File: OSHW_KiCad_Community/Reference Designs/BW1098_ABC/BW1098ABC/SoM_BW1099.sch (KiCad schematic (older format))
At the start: 29 parts

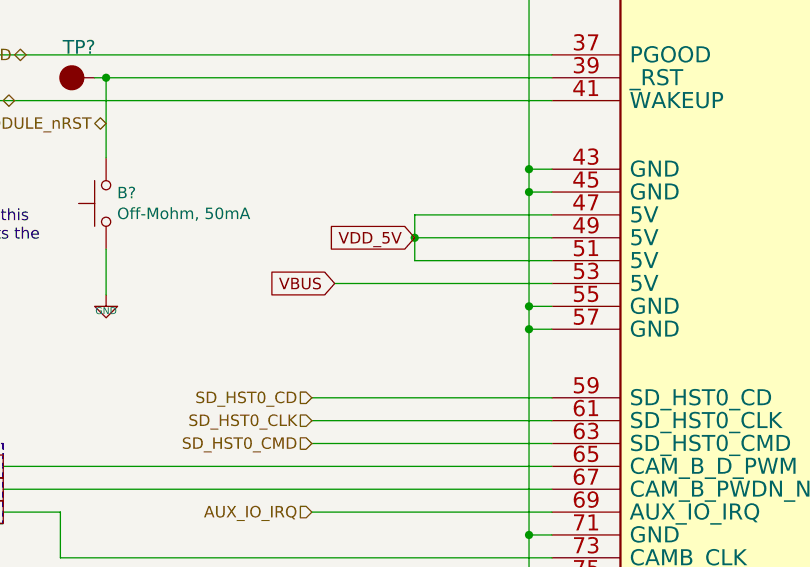
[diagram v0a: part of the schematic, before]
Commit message: skeleton complete, most footprints assigned, still need to check the transferred ones for dims
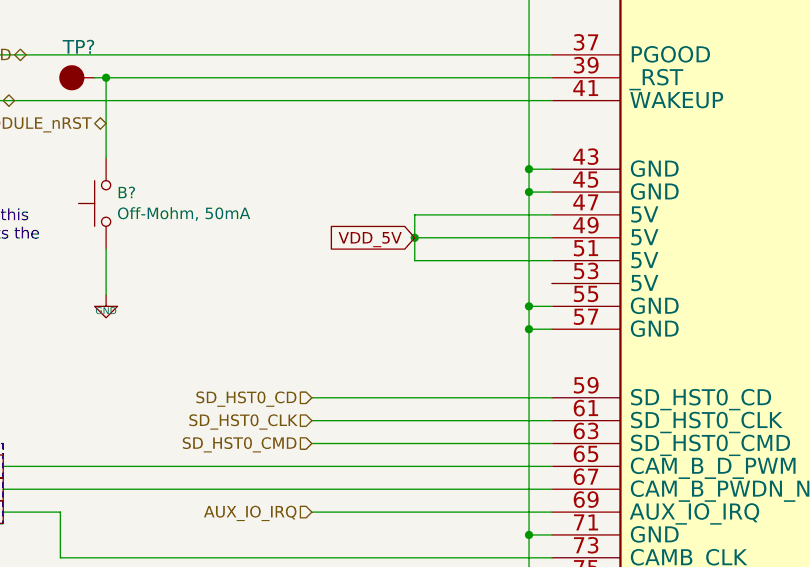
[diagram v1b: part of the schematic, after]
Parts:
- C?: footprint 0603 -> Capacitor_SMD:C_0201_0603Metric
- D? (x3): footprint (none) -> Diode_SMD:D_0201_0603Metric
- D?: footprint (none) -> Diode_SMD:D_SOD-523
- R? (x4): footprint (none) -> Resistor_SMD:R_0402_1005Metric
- R? (x2): footprint 0603 -> Resistor_SMD:R_0603_1608Metric
- TP? (x5): value BW1098OBC_Power_Supply-SchDoc-rescue_TEST_POINT- -> TEST_POINT; footprint (none) -> TestPoint:TestPoint_Loop_D1.80mm_Drill1.0mm_Beaded
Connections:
- net VBUS: no longer names the net of J?.53 (5V)
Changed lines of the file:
@@
 $Descr A3 16535 11693
 encoding utf-8
-Sheet 2 5
+Sheet 2 6
 Title ""
 Date ""
@@
 Wire Wire Line
 	7250 7600 4850 7600
-Wire Wire Line
-	6300 6000 7250 6000
 Wire Wire Line
 	10750 2900 9650 2900
@@
 AR Path="/5FF8D9B2/6009EFCC" Ref="TP?"  Part="1"
 F 0 "TP?" V 4283 5068 60  0000 C CNN
-F 1 "BW1098OBC_Power_Supply-SchDoc-rescue_TEST_POINT-" H 4230 5015 60  0001 L CNN
-F 2 "" H 4150 5000 60  0001 C CNN
+F 1 "TEST_POINT" H 4230 5015 60  0001 L CNN
+F 2 "TestPoint:TestPoint_Loop_D1.80mm_Drill1.0mm_Beaded" H 4150 5000 60  0001 C CNN
 F 3 "" H 4150 5000 60  0000 C CNN
 	1    4150 5000
@@
 AR Path="/5FF8D9B2/6009EFD2" Ref="TP?"  Part="1"
 F 0 "TP?" V 4283 5268 60  0000 C CNN
-F 1 "BW1098OBC_Power_Supply-SchDoc-rescue_TEST_POINT-" H 4230 5215 60  0001 L CNN
-F 2 "" H 4150 5200 60  0001 C CNN
+F 1 "TEST_POINT" H 4230 5215 60  0001 L CNN
+F 2 "TestPoint:TestPoint_Loop_D1.80mm_Drill1.0mm_Beaded" H 4150 5200 60  0001 C CNN
 F 3 "" H 4150 5200 60  0000 C CNN
 	1    4150 5200
@@
 AR Path="/5FF8D9B2/6009EFD8" Ref="TP?"  Part="1"
 F 0 "TP?" V 5383 5168 60  0000 C CNN
-F 1 "BW1098OBC_Power_Supply-SchDoc-rescue_TEST_POINT-" H 5330 5115 60  0001 L CNN
-F 2 "" H 5250 5100 60  0001 C CNN
+F 1 "TEST_POINT" H 5330 5115 60  0001 L CNN
+F 2 "TestPoint:TestPoint_Loop_D1.80mm_Drill1.0mm_Beaded" H 5250 5100 60  0001 C CNN
 F 3 "" H 5250 5100 60  0000 C CNN
 	1    5250 5100
@@
 AR Path="/5FF8D9B2/6009EFDE" Ref="TP?"  Part="1"
 F 0 "TP?" V 10250 6180 60  0000 L CNN
-F 1 "BW1098OBC_Power_Supply-SchDoc-rescue_TEST_POINT-" H 10330 6015 60  0001 L CNN
-F 2 "" H 10250 6000 60  0001 C CNN
+F 1 "TEST_POINT" H 10330 6015 60  0001 L CNN
+F 2 "TestPoint:TestPoint_Loop_D1.80mm_Drill1.0mm_Beaded" H 10250 6000 60  0001 C CNN
 F 3 "" H 10250 6000 60  0000 C CNN
 	1    10250 6000
@@
 F 0 "D?" V 1939 7632 50  0000 R CNN
 F 1 "ORANGE0603" V 1848 7632 50  0000 R CNN
-F 2 "" H 1900 7750 50  0001 C CNN
+F 2 "Diode_SMD:D_0201_0603Metric" H 1900 7750 50  0001 C CNN
 F 3 "~" H 1900 7750 50  0001 C CNN
 	1    1900 7750
@@
 F 0 "R?" H 1968 7396 50  0000 L CNN
 F 1 "1k 0402" H 1968 7305 50  0000 L CNN
-F 2 "" H 1900 7350 50  0001 C CNN
+F 2 "Resistor_SMD:R_0402_1005Metric" H 1900 7350 50  0001 C CNN
 F 3 "~" H 1900 7350 50  0001 C CNN
 	1    1900 7350
@@
 F 0 "D?" V 1889 5782 50  0000 R CNN
 F 1 "ORANGE0603" V 1798 5782 50  0000 R CNN
-F 2 "" H 1850 5900 50  0001 C CNN
+F 2 "Diode_SMD:D_0201_0603Metric" H 1850 5900 50  0001 C CNN
 F 3 "~" H 1850 5900 50  0001 C CNN
 	1    1850 5900
@@
 F 0 "R?" H 1918 5546 50  0000 L CNN
 F 1 "1k 0402" H 1918 5455 50  0000 L CNN
-F 2 "" H 1850 5500 50  0001 C CNN
+F 2 "Resistor_SMD:R_0402_1005Metric" H 1850 5500 50  0001 C CNN
 F 3 "~" H 1850 5500 50  0001 C CNN
 	1    1850 5500
@@
 F 0 "D?" V 1889 3482 50  0000 R CNN
 F 1 "RED0603" V 1798 3482 50  0000 R CNN
-F 2 "" H 1850 3600 50  0001 C CNN
+F 2 "Diode_SMD:D_0201_0603Metric" H 1850 3600 50  0001 C CNN
 F 3 "~" H 1850 3600 50  0001 C CNN
 	1    1850 3600
@@
 F 0 "R?" H 1918 3246 50  0000 L CNN
 F 1 "1k 0402" H 1918 3155 50  0000 L CNN
-F 2 "" H 1850 3200 50  0001 C CNN
+F 2 "Resistor_SMD:R_0402_1005Metric" H 1850 3200 50  0001 C CNN
 F 3 "~" H 1850 3200 50  0001 C CNN
 	1    1850 3200
@@
 F 0 "R?" H 1418 3146 50  0000 L CNN
 F 1 "1k 0402" H 1418 3055 50  0000 L CNN
-F 2 "" H 1350 3100 50  0001 C CNN
+F 2 "Resistor_SMD:R_0402_1005Metric" H 1350 3100 50  0001 C CNN
 F 3 "~" H 1350 3100 50  0001 C CNN
 	1    1350 3100
@@
 AR Path="/5FF8D9B2/6009F090" Ref="TP?"  Part="1"
 F 0 "TP?" H 10850 5350 60  0000 R CNN
-F 1 "BW1098OBC_Power_Supply-SchDoc-rescue_TEST_POINT-" H 11030 5215 60  0001 L CNN
-F 2 "" H 10950 5200 60  0001 C CNN
+F 1 "TEST_POINT" H 11030 5215 60  0001 L CNN
+F 2 "TestPoint:TestPoint_Loop_D1.80mm_Drill1.0mm_Beaded" H 10950 5200 60  0001 C CNN
 F 3 "" H 10950 5200 60  0000 C CNN
 	1    10950 5200
@@
 Text GLabel 4850 7000 0    50   UnSpc ~ 0
 CAM_B_CLK_OUT
-Text GLabel 6300 6000 0    50   Input ~ 0
-VBUS
 Text GLabel 6650 5800 0    50   Input ~ 0
 VDD_5V
@@
 F 0 "D?" H 13250 1143 50  0000 C CNN
 F 1 "BAS16XV2T1G" H 13250 1234 50  0000 C CNN
-F 2 "" H 13250 1275 50  0001 C CNN
-F 3 "" H 13250 1450 50  0001 C CNN
+F 2 "Diode_SMD:D_SOD-523" H 13250 1275 50  0001 C CNN
+F 3 "https://www.onsemi.com/pub/Collateral/BAS16XV2T1-D.PDF" H 13250 1450 50  0001 C CNN
 F 4 "DNP" H 13250 1325 50  0000 C CNN "Population"
 	1    13250 1450
@@
 F 0 "R?" V 13363 1718 45  0000 L CNN
 F 1 "10KOHM-0603" V 13550 1100 45  0000 L CNN
-F 2 "0603" H 13450 1800 20  0001 C CNN
+F 2 "Resistor_SMD:R_0603_1608Metric" H 13450 1800 20  0001 C CNN
 F 3 "" H 13450 1650 60  0001 C CNN
 F 4 "RES-00824" V 13534 1718 60  0001 L CNN "Field4"
@@
 F 0 "C?" H 14758 1995 45  0000 L CNN
 F 1 "4.7UF0603" H 14758 1911 45  0000 L CNN
-F 2 "0603" H 14650 2100 20  0001 C CNN
+F 2 "Capacitor_SMD:C_0201_0603Metric" H 14650 2100 20  0001 C CNN
 F 3 "" H 14650 1850 50  0001 C CNN
 F 4 "CAP-08280" H 14758 1816 60  0000 L CNN "Field4"
@@
 F 0 "R?" V 14650 1300 45  0000 L CNN
 F 1 "10KOHM-0603" V 14750 900 45  0000 L CNN
-F 2 "0603" H 14650 1600 20  0001 C CNN
+F 2 "Resistor_SMD:R_0603_1608Metric" H 14650 1600 20  0001 C CNN
 F 3 "" H 14650 1450 60  0001 C CNN
 F 4 "RES-00824" V 14734 1518 60  0001 L CNN "Field4"

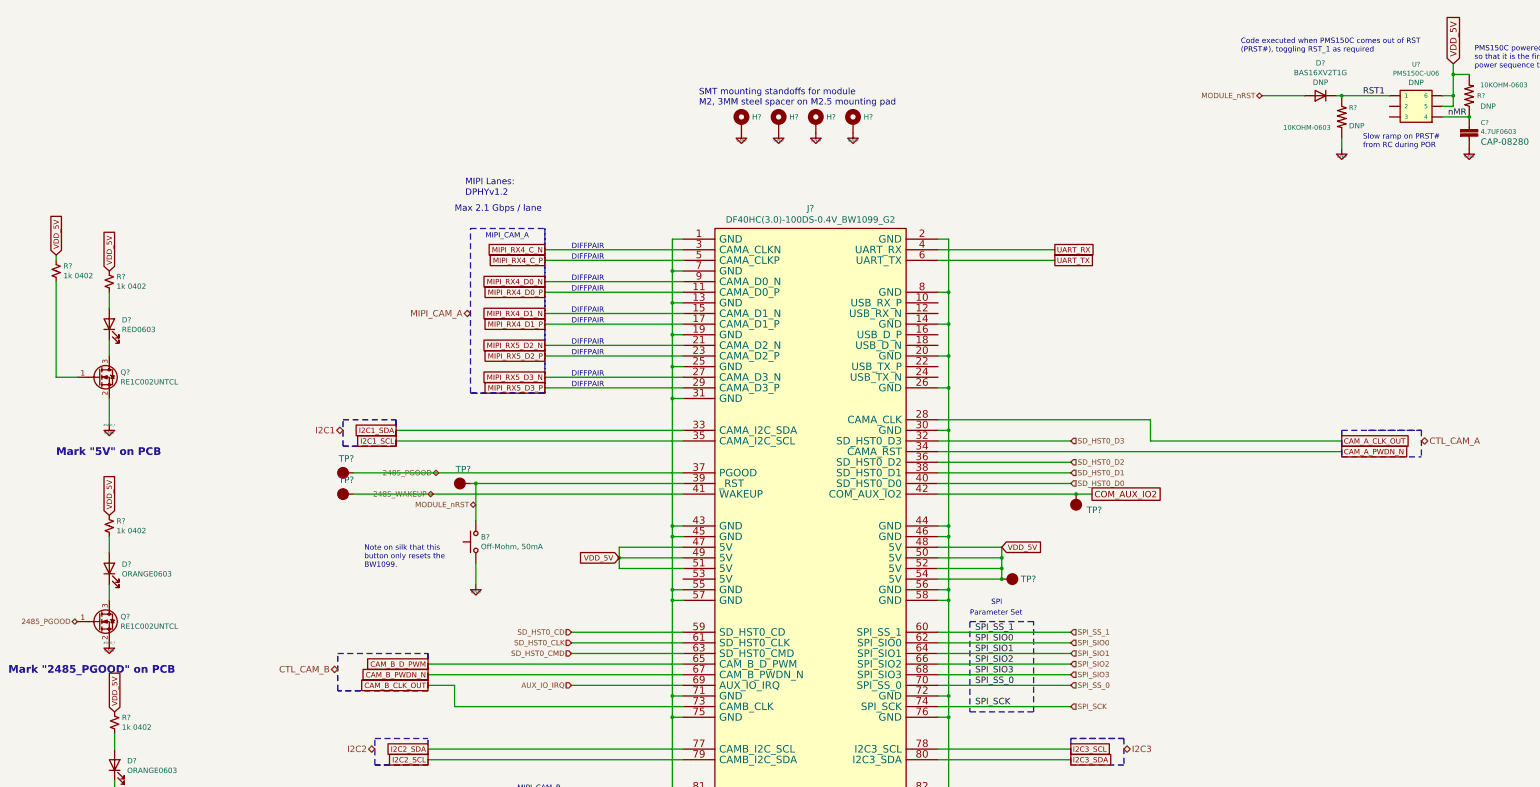
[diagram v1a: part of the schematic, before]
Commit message: schematic edits for BW1098ABC
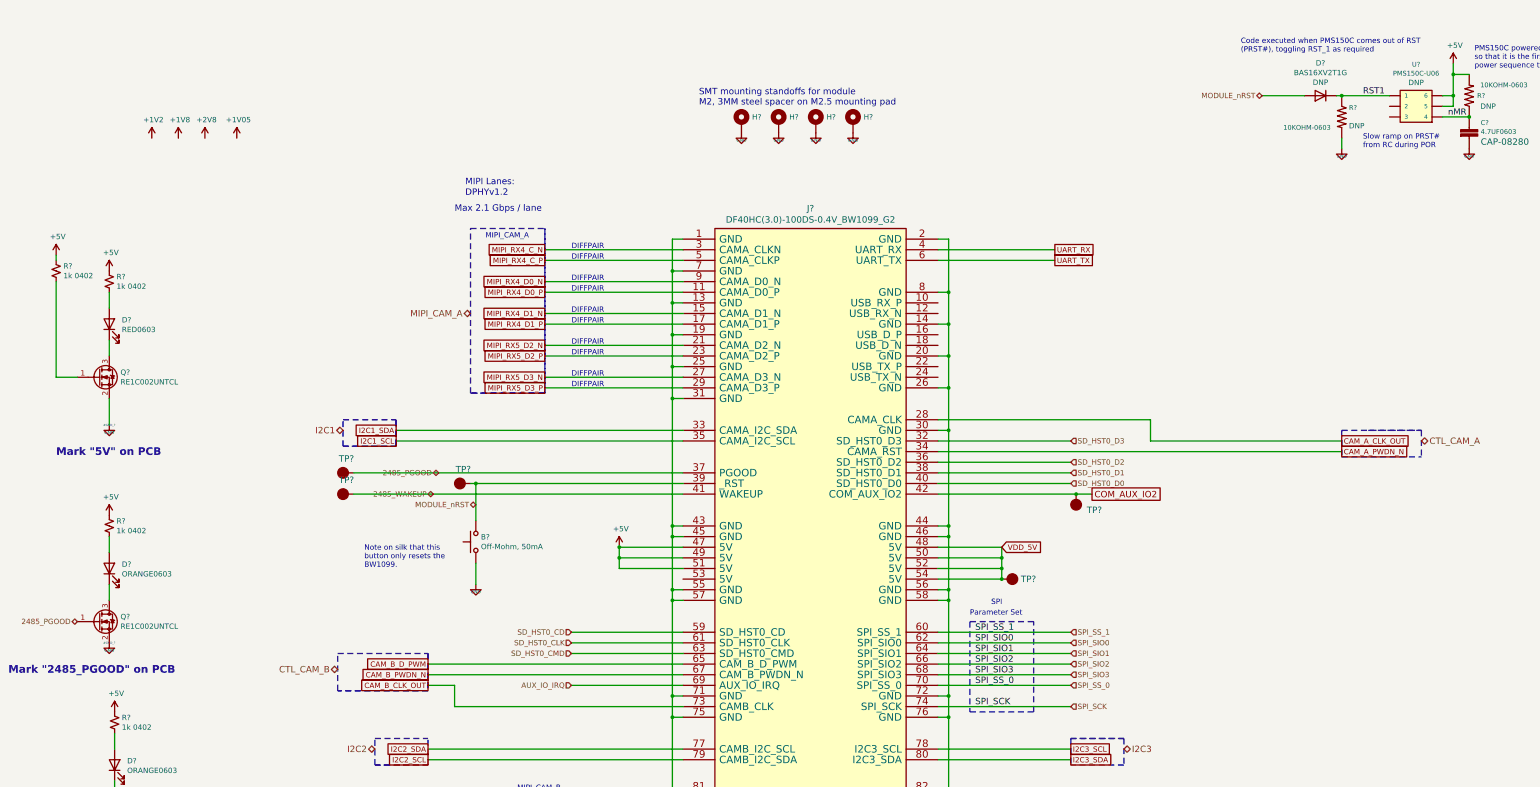
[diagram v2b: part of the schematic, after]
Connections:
- net VDD_5V: no longer J?.47 (5V), J?.49 (5V), J?.51 (5V), R?.1, R?.1, R?.1, R?.1, R?.2, U?.5, U?.6
- new net +5V: J?.47 (5V), J?.49 (5V), J?.51 (5V), R?.1, R?.1, R?.1, R?.1, R?.2, U?.5, U?.6
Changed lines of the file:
@@
 Text GLabel 4850 7000 0    50   UnSpc ~ 0
 CAM_B_CLK_OUT
-Text GLabel 6650 5800 0    50   Input ~ 0
-VDD_5V
 Text GLabel 4550 4600 0    50   UnSpc ~ 0
 I2C1_SDA
 Text GLabel 4550 4700 0    50   UnSpc ~ 0
 I2C1_SCL
-Text GLabel 1850 5400 1    50   Input ~ 0
-VDD_5V
-Text GLabel 1900 7250 1    50   Input ~ 0
-VDD_5V
-Text GLabel 1850 3100 1    50   Input ~ 0
-VDD_5V
-Text GLabel 1350 2950 1    50   Input ~ 0
-VDD_5V
 Text GLabel 5950 2900 0    50   UnSpc ~ 0
 MIPI_RX4_C_N
@@
 $EndComp
 Connection ~ 14650 1650
-Text GLabel 14500 1150 1    60   Input ~ 0
-VDD_5V
 Wire Wire Line
 	14650 1250 14500 1250
@@
 Wire Wire Line
 	10500 8800 9650 8800
+$Comp
+L power:+5V #PWR?
+U 1 1 60025A18
+P 1350 2950
+AR Path="/604AEAFA/60025A18" Ref="#PWR?"  Part="1"
+AR Path="/5FF8D9B2/60025A18" Ref="#PWR?"  Part="1"
+F 0 "#PWR?" H 1350 2800 50  0001 C CNN
+F 1 "+5V" H 1365 3123 50  0000 C CNN
+F 2 "" H 1350 2950 50  0001 C CNN
+F 3 "" H 1350 2950 50  0001 C CNN
+	1    1350 2950
+	1    0    0    -1
+$EndComp
+$Comp
+L power:+1V2 #PWR?
+U 1 1 60025A1E
+P 2250 1850
+F 0 "#PWR?" H 2250 1700 50  0001 C CNN
+F 1 "+1V2" H 2265 2023 50  0000 C CNN
+F 2 "" H 2250 1850 50  0001 C CNN
+F 3 "" H 2250 1850 50  0001 C CNN
+	1    2250 1850
+	1    0    0    -1
+$EndComp
+$Comp
+L power:+1V8 #PWR?
+U 1 1 60025A24
+P 2500 1850
+F 0 "#PWR?" H 2500 1700 50  0001 C CNN
+F 1 "+1V8" H 2515 2023 50  0000 C CNN
+F 2 "" H 2500 1850 50  0001 C CNN
+F 3 "" H 2500 1850 50  0001 C CNN
+	1    2500 1850
+	1    0    0    -1
+$EndComp
+$Comp
+L power:+2V8 #PWR?
+U 1 1 60025A2A
+P 2750 1850
+F 0 "#PWR?" H 2750 1700 50  0001 C CNN
+F 1 "+2V8" H 2765 2023 50  0000 C CNN
+F 2 "" H 2750 1850 50  0001 C CNN
+F 3 "" H 2750 1850 50  0001 C CNN
+	1    2750 1850
+	1    0    0    -1
+$EndComp
+$Comp
+L depthAI_sch:+1V05 #PWR?
+U 1 1 60025A30
+P 3050 1850
+F 0 "#PWR?" H 3050 1700 50  0001 C CNN
+F 1 "+1V05" H 3065 2023 50  0000 C CNN
+F 2 "" H 3050 1850 50  0001 C CNN
+F 3 "" H 3050 1850 50  0001 C CNN
+	1    3050 1850
+	1    0    0    -1
+$EndComp
+$Comp
+L power:+5V #PWR?
+U 1 1 600461B4
+P 1850 3100
+AR Path="/604AEAFA/600461B4" Ref="#PWR?"  Part="1"
+AR Path="/5FF8D9B2/600461B4" Ref="#PWR?"  Part="1"
+F 0 "#PWR?" H 1850 2950 50  0001 C CNN
+F 1 "+5V" H 1865 3273 50  0000 C CNN
+F 2 "" H 1850 3100 50  0001 C CNN
+F 3 "" H 1850 3100 50  0001 C CNN
+	1    1850 3100
+	1    0    0    -1
+$EndComp
+$Comp
+L power:+5V #PWR?
+U 1 1 6004658E
+P 1850 5400
+AR Path="/604AEAFA/6004658E" Ref="#PWR?"  Part="1"
+AR Path="/5FF8D9B2/6004658E" Ref="#PWR?"  Part="1"
+F 0 "#PWR?" H 1850 5250 50  0001 C CNN
+F 1 "+5V" H 1865 5573 50  0000 C CNN
+F 2 "" H 1850 5400 50  0001 C CNN
+F 3 "" H 1850 5400 50  0001 C CNN
+	1    1850 5400
+	1    0    0    -1
+$EndComp
+$Comp
+L power:+5V #PWR?
+U 1 1 60051547
+P 1900 7250
+AR Path="/604AEAFA/60051547" Ref="#PWR?"  Part="1"
+AR Path="/5FF8D9B2/60051547" Ref="#PWR?"  Part="1"
+F 0 "#PWR?" H 1900 7100 50  0001 C CNN
+F 1 "+5V" H 1915 7423 50  0000 C CNN
+F 2 "" H 1900 7250 50  0001 C CNN
+F 3 "" H 1900 7250 50  0001 C CNN
+	1    1900 7250
+	1    0    0    -1
+$EndComp
+$Comp
+L power:+5V #PWR?
+U 1 1 60051B26
+P 6650 5700
+AR Path="/604AEAFA/60051B26" Ref="#PWR?"  Part="1"
+AR Path="/5FF8D9B2/60051B26" Ref="#PWR?"  Part="1"
+F 0 "#PWR?" H 6650 5550 50  0001 C CNN
+F 1 "+5V" H 6665 5873 50  0000 C CNN
+F 2 "" H 6650 5700 50  0001 C CNN
+F 3 "" H 6650 5700 50  0001 C CNN
+	1    6650 5700
+	1    0    0    -1
+$EndComp
+Connection ~ 6650 5700
+$Comp
+L power:+5V #PWR?
+U 1 1 60072499
+P 14500 1150
+AR Path="/604AEAFA/60072499" Ref="#PWR?"  Part="1"
+AR Path="/5FF8D9B2/60072499" Ref="#PWR?"  Part="1"
+F 0 "#PWR?" H 14500 1000 50  0001 C CNN
+F 1 "+5V" H 14515 1323 50  0000 C CNN
+F 2 "" H 14500 1150 50  0001 C CNN
+F 3 "" H 14500 1150 50  0001 C CNN
+	1    14500 1150
+	1    0    0    -1
+$EndComp
 $EndSCHEMATC

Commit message: small stuff
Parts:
- C?: symbol SparkFun-Capacitors:4.7UF0603 -> BW1098ABC-rescue:4.7UF0603-SparkFun-Capacitors; Voltage Rating (none) -> 10V
- J? (x3): symbol depthAI_sch:20021121-00010T1LF -> BW1098ABC-rescue:20021121-00010T1LF-depthAI_sch
- J?: symbol depthAI_sch:DF40HC(3.0)-100DS-0.4V_BW1099_G2 -> BW1098ABC-rescue:DF40HC(3.0)-100DS-0.4V_BW1099_G2-depthAI_sch
- R? (x2): symbol SparkFun-Resistors:10KOHM-0603-1_10W-1% -> BW1098ABC-rescue:10KOHM-0603-1_10W-1%-SparkFun-Resistors
- TP? (x5): symbol depthAI_sch:TEST_POINT -> BW1098ABC-rescue:TEST_POINT-depthAI_sch
- U?: symbol depthAI_sch:PMS150C-U06 -> BW1098ABC-rescue:PMS150C-U06-depthAI_sch
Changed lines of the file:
@@
 SPI
 $Comp
-L depthAI_sch:TEST_POINT TP?
+L BW1098ABC-rescue:TEST_POINT-depthAI_sch TP?
 U 1 1 6009EFCC
 P 4150 5000
@@
 $EndComp
 $Comp
-L depthAI_sch:TEST_POINT TP?
+L BW1098ABC-rescue:TEST_POINT-depthAI_sch TP?
 U 1 1 6009EFD2
 P 4150 5200
@@
 $EndComp
 $Comp
-L depthAI_sch:TEST_POINT TP?
+L BW1098ABC-rescue:TEST_POINT-depthAI_sch TP?
 U 1 1 6009EFD8
 P 5250 5100
@@
 $EndComp
 $Comp
-L depthAI_sch:TEST_POINT TP?
+L BW1098ABC-rescue:TEST_POINT-depthAI_sch TP?
 U 1 1 6009EFDE
 P 10250 6000
@@
 2485_PGOOD and MODULE_nRST both have pull ups to 1.8V \non 1099 module. 2485_PGOOD is held low by open-drain output \non 1099 PMIC until power is good. MODULE_nRST rises with \n1.8V at POR, but can be held low by user button or 1099 JTAG.
 $Comp
-L depthAI_sch:20021121-00010T1LF J?
+L BW1098ABC-rescue:20021121-00010T1LF-depthAI_sch J?
 U 1 1 6009EFE6
 P 4150 10350
@@
 $EndComp
 $Comp
-L depthAI_sch:20021121-00010T1LF J?
+L BW1098ABC-rescue:20021121-00010T1LF-depthAI_sch J?
 U 1 1 6009EFED
 P 7050 10350
@@
 $EndComp
 $Comp
-L depthAI_sch:20021121-00010T1LF J?
+L BW1098ABC-rescue:20021121-00010T1LF-depthAI_sch J?
 U 1 1 6009EFF4
 P 10100 10350
@@
 	13450 4600 13450 4850
 $Comp
-L depthAI_sch:DF40HC(3.0)-100DS-0.4V_BW1099_G2 J?
+L BW1098ABC-rescue:DF40HC(3.0)-100DS-0.4V_BW1099_G2-depthAI_sch J?
 U 1 1 6009F08A
 P 7250 2800
@@
 $EndComp
 $Comp
-L depthAI_sch:TEST_POINT TP?
+L BW1098ABC-rescue:TEST_POINT-depthAI_sch TP?
 U 1 1 6009F090
 P 10950 5200
@@
 RST1
 $Comp
-L SparkFun-Resistors:10KOHM-0603-1_10W-1% R?
+L BW1098ABC-rescue:10KOHM-0603-1_10W-1%-SparkFun-Resistors R?
 U 1 1 6009F10D
 P 13450 1650
@@
 $EndComp
 $Comp
-L SparkFun-Capacitors:4.7UF0603 C?
+L BW1098ABC-rescue:4.7UF0603-SparkFun-Capacitors C?
 U 1 1 6009F123
 P 14650 1850
 AR Path="/5FD7EFCD/6009F123" Ref="C?"  Part="1"
 AR Path="/5FF8D9B2/6009F123" Ref="C?"  Part="1"
+AR Path="/6009F123" Ref="C?"  Part="1"
 F 0 "C?" H 14758 1995 45  0000 L CNN
 F 1 "4.7UF0603" H 14758 1911 45  0000 L CNN
@@
 F 3 "" H 14650 1850 50  0001 C CNN
 F 4 "CAP-08280" H 14758 1816 60  0000 L CNN "Field4"
+F 5 "10V" H 14650 1850 50  0001 C CNN "Voltage Rating"
 	1    14650 1850
 	1    0    0    -1
@@
 	14650 1650 14400 1650
 $Comp
-L depthAI_sch:PMS150C-U06 U?
+L BW1098ABC-rescue:PMS150C-U06-depthAI_sch U?
 U 1 1 6009F12B
 P 14150 1550
@@
 nMR
 $Comp
-L SparkFun-Resistors:10KOHM-0603-1_10W-1% R?
+L BW1098ABC-rescue:10KOHM-0603-1_10W-1%-SparkFun-Resistors R?
 U 1 1 6009F135
 P 14650 1450
@@
 $EndComp
 $Comp
-L depthAI_sch:+1V05 #PWR?
+L BW1098ABC-rescue:+1V05-depthAI_sch #PWR?
 U 1 1 60025A30
 P 3050 1850

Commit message: all footprints associated on bw1098abc board except two I need to clarify with Brian. Need to talk to chris about power
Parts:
- B?: footprint (none) -> DTSM-32N-V-T_R:DTSM32NVTR
- C?: footprint Capacitor_SMD:C_0201_0603Metric -> Capacitor_SMD:C_0603_1608Metric
- D? (x2): footprint Diode_SMD:D_0201_0603Metric -> Diode_SMD:D_0603_1608Metric
- Q? (x3): footprint (none) -> OSHW_LuxonisMaster_20201223:RE1C002UNTCL
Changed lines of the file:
@@
 F 0 "B?" V 5346 5602 50  0000 R CNN
 F 1 "Off-Mohm, 50mA" V 5255 5602 50  0000 R CNN
-F 2 "" H 5300 5850 50  0001 C CNN
+F 2 "DTSM-32N-V-T_R:DTSM32NVTR" H 5300 5850 50  0001 C CNN
 F 3 "http://www.apem.com/int/index.php?controller=attachment&id_attachment=488" H 5300 5850 50  0001 C CNN
 	1    5300 5650
@@
 F 0 "D?" V 1939 7632 50  0000 R CNN
 F 1 "ORANGE0603" V 1848 7632 50  0000 R CNN
-F 2 "Diode_SMD:D_0201_0603Metric" H 1900 7750 50  0001 C CNN
+F 2 "Diode_SMD:D_0603_1608Metric" H 1900 7750 50  0001 C CNN
 F 3 "~" H 1900 7750 50  0001 C CNN
 	1    1900 7750
@@
 F 0 "Q?" H 2005 8296 50  0000 L CNN
 F 1 "RE1C002UNTCL" H 2005 8205 50  0000 L CNN
-F 2 "" H 2000 8350 50  0001 C CNN
+F 2 "OSHW_LuxonisMaster_20201223:RE1C002UNTCL" H 2000 8350 50  0001 C CNN
 F 3 "~" H 1800 8250 50  0001 C CNN
 	1    1800 8250
@@
 F 0 "D?" V 1889 5782 50  0000 R CNN
 F 1 "ORANGE0603" V 1798 5782 50  0000 R CNN
-F 2 "Diode_SMD:D_0201_0603Metric" H 1850 5900 50  0001 C CNN
+F 2 "Diode_SMD:D_0603_1608Metric" H 1850 5900 50  0001 C CNN
 F 3 "~" H 1850 5900 50  0001 C CNN
 	1    1850 5900
@@
 F 0 "Q?" H 1955 6446 50  0000 L CNN
 F 1 "RE1C002UNTCL" H 1955 6355 50  0000 L CNN
-F 2 "" H 1950 6500 50  0001 C CNN
+F 2 "OSHW_LuxonisMaster_20201223:RE1C002UNTCL" H 1950 6500 50  0001 C CNN
 F 3 "~" H 1750 6400 50  0001 C CNN
 	1    1750 6400
@@
 F 0 "Q?" H 1955 4146 50  0000 L CNN
 F 1 "RE1C002UNTCL" H 1955 4055 50  0000 L CNN
-F 2 "" H 1950 4200 50  0001 C CNN
+F 2 "OSHW_LuxonisMaster_20201223:RE1C002UNTCL" H 1950 4200 50  0001 C CNN
 F 3 "~" H 1750 4100 50  0001 C CNN
 	1    1750 4100
@@
 F 0 "C?" H 14758 1995 45  0000 L CNN
 F 1 "4.7UF0603" H 14758 1911 45  0000 L CNN
-F 2 "Capacitor_SMD:C_0201_0603Metric" H 14650 2100 20  0001 C CNN
+F 2 "Capacitor_SMD:C_0603_1608Metric" H 14650 2100 20  0001 C CNN
 F 3 "" H 14650 1850 50  0001 C CNN
 F 4 "CAP-08280" H 14758 1816 60  0000 L CNN "Field4"
